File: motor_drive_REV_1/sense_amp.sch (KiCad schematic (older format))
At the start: 4 parts

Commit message: work on component libraries and schematic
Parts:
- removed C?: C, symbol Device:C
- removed R? (x2): R, symbol Device:R
- removed U?: AD8418, symbol motor_drive:AD8418
- added C?: C, symbol Device:C
- added U?: AD8418ABRMZ-RL, RM_8, symbol motor_drive:AD8418ABRMZ-RL
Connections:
- net labels added: 5.0V, OUT
- net labels removed: VCC, out
- wire segments 12 -> 10
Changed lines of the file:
@@
 $Descr A4 11693 8268
 encoding utf-8
-Sheet 9 14
+Sheet 13 14
 Title ""
 Date ""
@@
 Comment4 ""
 $EndDescr
+Text HLabel 6500 3500 2    50   Input ~ 0
+IN+
+Text HLabel 4500 3500 0    50   Input ~ 0
+IN-
 $Comp
-L Device:R R?
-U 1 1 5E23D4AE
-P 5850 1800
-AR Path="/5E1E8A88/5E23D4AE" Ref="R?"  Part="1"
-AR Path="/5E23C306/5E23D4AE" Ref="R?"  Part="1"
-AR Path="/5E285F18/5E23D4AE" Ref="R?"  Part="1"
-AR Path="/5E286BCF/5E23D4AE" Ref="R?"  Part="1"
-AR Path="/5E291A12/5E23D4AE" Ref="R?"  Part="1"
-AR Path="/5E2938C8/5E23D4AE" Ref="R?"  Part="1"
-AR Path="/5E295828/5E23D4AE" Ref="R?"  Part="1"
-AR Path="/5E2E3D6E/5E23D4AE" Ref="R?"  Part="1"
-AR Path="/5E2E5BBE/5E23D4AE" Ref="R?"  Part="1"
-AR Path="/5E2E7F62/5E23D4AE" Ref="R?"  Part="1"
-F 0 "R?" H 5920 1846 50  0000 L CNN
-F 1 "R" H 5920 1755 50  0000 L CNN
-F 2 "" V 5780 1800 50  0001 C CNN
-F 3 "~" H 5850 1800 50  0001 C CNN
-	1    5850 1800
-	1    0    0    -1
-$EndComp
-$Comp
-L Device:R R?
-U 1 1 5E23D4B4
-P 6350 1800
-AR Path="/5E1E8A88/5E23D4B4" Ref="R?"  Part="1"
-AR Path="/5E23C306/5E23D4B4" Ref="R?"  Part="1"
-AR Path="/5E285F18/5E23D4B4" Ref="R?"  Part="1"
-AR Path="/5E286BCF/5E23D4B4" Ref="R?"  Part="1"
-AR Path="/5E291A12/5E23D4B4" Ref="R?"  Part="1"
-AR Path="/5E2938C8/5E23D4B4" Ref="R?"  Part="1"
-AR Path="/5E295828/5E23D4B4" Ref="R?"  Part="1"
-AR Path="/5E2E3D6E/5E23D4B4" Ref="R?"  Part="1"
-AR Path="/5E2E5BBE/5E23D4B4" Ref="R?"  Part="1"
-AR Path="/5E2E7F62/5E23D4B4" Ref="R?"  Part="1"
-F 0 "R?" H 6420 1846 50  0000 L CNN
-F 1 "R" H 6420 1755 50  0000 L CNN
-F 2 "" V 6280 1800 50  0001 C CNN
-F 3 "~" H 6350 1800 50  0001 C CNN
-	1    6350 1800
-	1    0    0    -1
-$EndComp
-$Comp
-L Device:C C?
-U 1 1 5E23D4BA
-P 5100 4600
-AR Path="/5E1E8A88/5E23D4BA" Ref="C?"  Part="1"
-AR Path="/5E23C306/5E23D4BA" Ref="C?"  Part="1"
-AR Path="/5E285F18/5E23D4BA" Ref="C?"  Part="1"
-AR Path="/5E286BCF/5E23D4BA" Ref="C?"  Part="1"
-AR Path="/5E291A12/5E23D4BA" Ref="C?"  Part="1"
-AR Path="/5E2938C8/5E23D4BA" Ref="C?"  Part="1"
-AR Path="/5E295828/5E23D4BA" Ref="C?"  Part="1"
-AR Path="/5E2E3D6E/5E23D4BA" Ref="C?"  Part="1"
-AR Path="/5E2E5BBE/5E23D4BA" Ref="C?"  Part="1"
-AR Path="/5E2E7F62/5E23D4BA" Ref="C?"  Part="1"
-F 0 "C?" H 5215 4646 50  0000 L CNN
-F 1 "C" H 5215 4555 50  0000 L CNN
-F 2 "" H 5138 4450 50  0001 C CNN
-F 3 "~" H 5100 4600 50  0001 C CNN
-	1    5100 4600
-	0    -1   -1   0
-$EndComp
-$Comp
-L power:GND #PWR?
-U 1 1 5E23E102
-P 5850 4750
-AR Path="/5E23C306/5E23E102" Ref="#PWR?"  Part="1"
-AR Path="/5E285F18/5E23E102" Ref="#PWR?"  Part="1"
-AR Path="/5E286BCF/5E23E102" Ref="#PWR?"  Part="1"
-AR Path="/5E291A12/5E23E102" Ref="#PWR?"  Part="1"
-AR Path="/5E2938C8/5E23E102" Ref="#PWR?"  Part="1"
-AR Path="/5E295828/5E23E102" Ref="#PWR?"  Part="1"
-AR Path="/5E2E3D6E/5E23E102" Ref="#PWR?"  Part="1"
-AR Path="/5E2E5BBE/5E23E102" Ref="#PWR?"  Part="1"
-AR Path="/5E2E7F62/5E23E102" Ref="#PWR?"  Part="1"
-F 0 "#PWR?" H 5850 4500 50  0001 C CNN
-F 1 "GND" H 5855 4577 50  0000 C CNN
-F 2 "" H 5850 4750 50  0001 C CNN
-F 3 "" H 5850 4750 50  0001 C CNN
-	1    5850 4750
-	1    0    0    -1
-$EndComp
-Text HLabel 5750 3700 2    50   Input ~ 0
-out
-Wire Wire Line
-	5750 3800 5850 3800
-Wire Wire Line
-	5350 4100 5350 4600
-Wire Wire Line
-	5350 4600 5250 4600
-Wire Wire Line
-	5350 4600 5850 4600
-Connection ~ 5350 4600
-Connection ~ 5850 4600
-Wire Wire Line
-	5850 4600 5850 4750
-Wire Wire Line
-	5850 3800 5850 4600
-Wire Wire Line
-	4950 3800 4750 3800
-Wire Wire Line
-	4750 3800 4750 3900
-Wire Wire Line
-	4750 4600 4950 4600
-Wire Wire Line
-	4950 3900 4750 3900
-Connection ~ 4750 3900
-Wire Wire Line
-	4750 3900 4750 4600
-$Comp
-L power:VCC #PWR?
-U 1 1 5E2423AC
-P 4750 3600
-AR Path="/5E23C306/5E2423AC" Ref="#PWR?"  Part="1"
-AR Path="/5E285F18/5E2423AC" Ref="#PWR?"  Part="1"
-AR Path="/5E286BCF/5E2423AC" Ref="#PWR?"  Part="1"
-AR Path="/5E291A12/5E2423AC" Ref="#PWR?"  Part="1"
-AR Path="/5E2938C8/5E2423AC" Ref="#PWR?"  Part="1"
-AR Path="/5E295828/5E2423AC" Ref="#PWR?"  Part="1"
-AR Path="/5E2E3D6E/5E2423AC" Ref="#PWR?"  Part="1"
-AR Path="/5E2E5BBE/5E2423AC" Ref="#PWR?"  Part="1"
-AR Path="/5E2E7F62/5E2423AC" Ref="#PWR?"  Part="1"
-F 0 "#PWR?" H 4750 3450 50  0001 C CNN
-F 1 "VCC" H 4767 3773 50  0000 C CNN
-F 2 "" H 4750 3600 50  0001 C CNN
-F 3 "" H 4750 3600 50  0001 C CNN
-	1    4750 3600
+L motor_drive:AD8418ABRMZ-RL U?
+U 1 1 5E259F13
+P 4500 3500
+AR Path="/5E291A12/5E259F13" Ref="U?"  Part="1"
+AR Path="/5E2938C8/5E259F13" Ref="U?"  Part="1"
+AR Path="/5E295828/5E259F13" Ref="U?"  Part="1"
+AR Path="/5E2E3D6E/5E259F13" Ref="U?"  Part="1"
+AR Path="/5E2E5BBE/5E259F13" Ref="U?"  Part="1"
+AR Path="/5E2E7F62/5E259F13" Ref="U?"  Part="1"
+AR Path="/5E336639/5E259F13" Ref="U?"  Part="1"
+AR Path="/5E33A08D/5E259F13" Ref="U?"  Part="1"
+AR Path="/5E33E36D/5E259F13" Ref="U?"  Part="1"
+F 0 "U?" H 5500 3887 60  0000 C CNN
+F 1 "AD8418ABRMZ-RL" H 5500 3781 60  0000 C CNN
+F 2 "RM_8" H 5500 3740 60  0001 C CNN
+F 3 "" H 4500 3500 60  0000 C CNN
+	1    4500 3500
 	1    0    0    -1
 $EndComp
 Wire Wire Line
-	4750 3600 4750 3800
-Connection ~ 4750 3800
-Text HLabel 5150 3300 1    50   Input ~ 0
-IN+
-Text HLabel 5550 3300 1    50   Input ~ 0
-IN-
-Text HLabel 5850 4600 2    50   Input ~ 0
+	4500 3600 4100 3600
+Wire Wire Line
+	4500 3700 4100 3700
+Wire Wire Line
+	4100 3600 4100 3700
+Wire Wire Line
+	7150 3600 6500 3600
+Wire Wire Line
+	6500 3700 7150 3700
+Wire Wire Line
+	7150 3700 7150 3600
+$Comp
+L Device:C C?
+U 1 1 5E25CC80
+P 5500 4250
+AR Path="/5E1E8A88/5E25CC80" Ref="C?"  Part="1"
+AR Path="/5E23C306/5E25CC80" Ref="C?"  Part="1"
+AR Path="/5E285F18/5E25CC80" Ref="C?"  Part="1"
+AR Path="/5E286BCF/5E25CC80" Ref="C?"  Part="1"
+AR Path="/5E291A12/5E25CC80" Ref="C?"  Part="1"
+AR Path="/5E2938C8/5E25CC80" Ref="C?"  Part="1"
+AR Path="/5E295828/5E25CC80" Ref="C?"  Part="1"
+AR Path="/5E2E3D6E/5E25CC80" Ref="C?"  Part="1"
+AR Path="/5E2E5BBE/5E25CC80" Ref="C?"  Part="1"
+AR Path="/5E2E7F62/5E25CC80" Ref="C?"  Part="1"
+AR Path="/5E336639/5E25CC80" Ref="C?"  Part="1"
+AR Path="/5E33A08D/5E25CC80" Ref="C?"  Part="1"
+AR Path="/5E33E36D/5E25CC80" Ref="C?"  Part="1"
+F 0 "C?" H 5615 4296 50  0000 L CNN
+F 1 "C" H 5615 4205 50  0000 L CNN
+F 2 "" H 5538 4100 50  0001 C CNN
+F 3 "~" H 5500 4250 50  0001 C CNN
+	1    5500 4250
+	0    -1   -1   0
+$EndComp
+Wire Wire Line
+	4100 3700 4100 4250
+Connection ~ 4100 3700
+Wire Wire Line
+	5350 4250 4100 4250
+Wire Wire Line
+	5650 4250 7150 4250
+Wire Wire Line
+	7150 4250 7150 3700
+Connection ~ 7150 3700
+Text HLabel 6500 3800 2    50   Input ~ 0
+OUT
+Text HLabel 7150 3600 2    50   Input ~ 0
+5.0V
+Text HLabel 4100 4250 0    50   Input ~ 0
 GND
-Text HLabel 4750 3800 0    50   Input ~ 0
-VCC
-$Comp
-L motor_drive:AD8418 U?
-U 1 1 5E24089B
-P 5350 3700
-F 0 "U?" H 5350 3211 50  0000 C CNN
-F 1 "AD8418" H 5350 3120 50  0000 C CNN
-F 2 "" H 5400 3350 50  0001 C CNN
-F 3 "https://www.analog.com/media/en/technical-documentation/data-sheets/AD8418.pdf" H 6000 3000 50  0001 C CNN
-	1    5350 3700
-	1    0    0    -1
-$EndComp
 $EndSCHEMATC

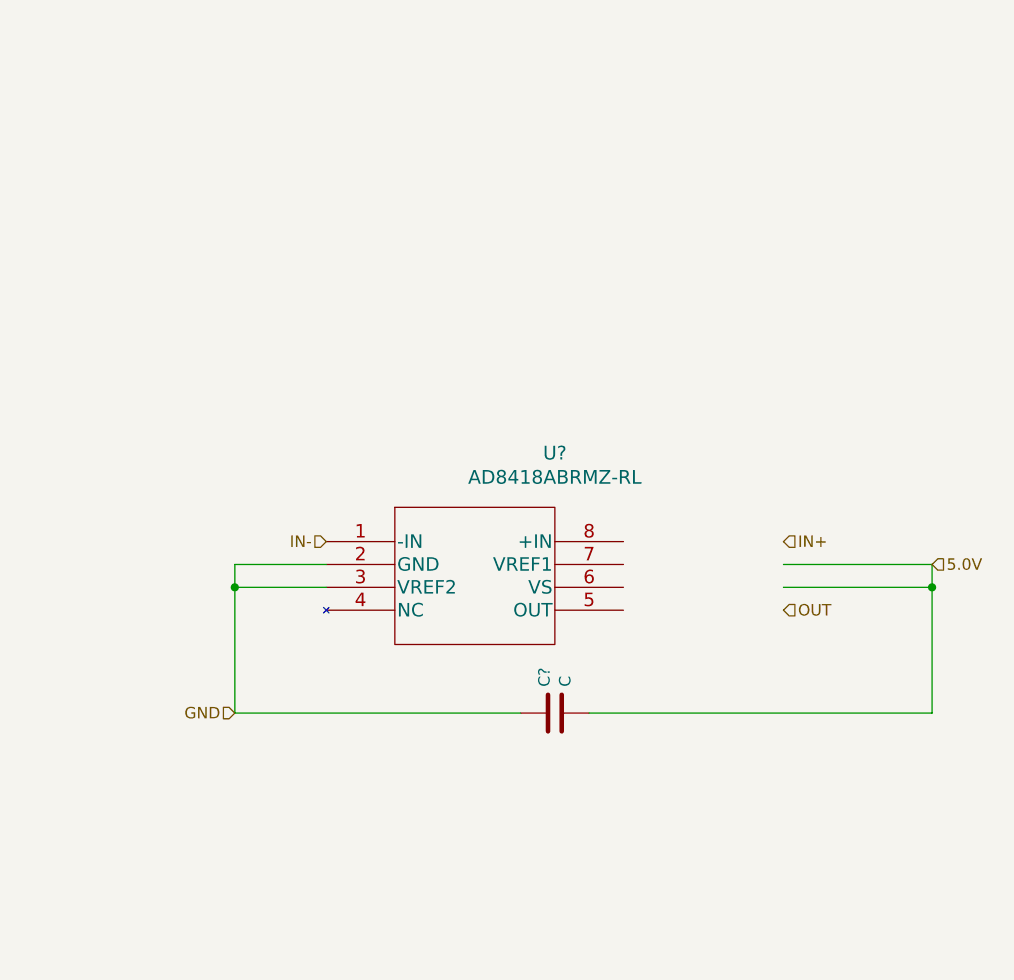
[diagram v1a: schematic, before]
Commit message: organizing pinout and BOM
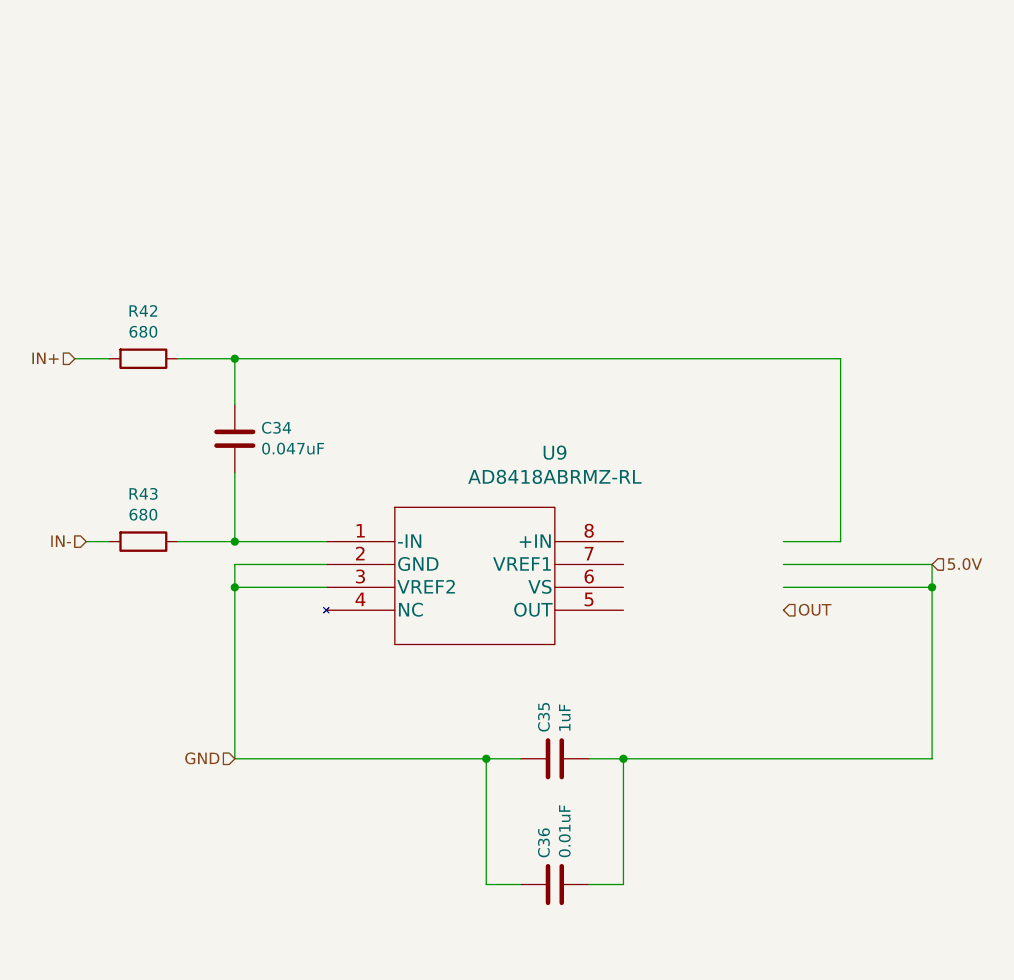
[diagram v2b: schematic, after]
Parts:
- added C1: 0.047uF, motor_drive_footprints:C_0603_1608Metric, symbol motor_drive:C
- added C36: 0.01uF, motor_drive_footprints:C_0603_1608Metric, symbol Device:C
- added R10, R11: 680, motor_drive_footprints:C_0603_1608Metric, symbol motor_drive:R
- C35: renamed from C?; value C -> 1uF; footprint (none) -> motor_drive_footprints:C_0603_1608Metric
- U9: renamed from U?; footprint RM_8 -> motor_drive_footprints:AD8418ABRMZ-RL
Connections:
- wire segments 10 -> 26
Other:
- moved on the sheet: C35
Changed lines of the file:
@@
 $Descr A4 11693 8268
 encoding utf-8
-Sheet 13 14
+Sheet 14 14
 Title ""
 Date ""
@@
 Comment4 ""
 $EndDescr
-Text HLabel 6500 3500 2    50   Input ~ 0
+Text HLabel 3400 2700 0    50   Input ~ 0
 IN+
-Text HLabel 4500 3500 0    50   Input ~ 0
-IN-
-$Comp
-L motor_drive:AD8418ABRMZ-RL U?
+$Comp
+L motor_drive:AD8418ABRMZ-RL U9
 U 1 1 5E259F13
 P 4500 3500
-AR Path="/5E291A12/5E259F13" Ref="U?"  Part="1"
-AR Path="/5E2938C8/5E259F13" Ref="U?"  Part="1"
-AR Path="/5E295828/5E259F13" Ref="U?"  Part="1"
+AR Path="/5E291A12/5E259F13" Ref="U9"  Part="1"
+AR Path="/5E2938C8/5E259F13" Ref="U1"  Part="1"
+AR Path="/5E295828/5E259F13" Ref="U2"  Part="1"
 AR Path="/5E2E3D6E/5E259F13" Ref="U?"  Part="1"
 AR Path="/5E2E5BBE/5E259F13" Ref="U?"  Part="1"
 AR Path="/5E2E7F62/5E259F13" Ref="U?"  Part="1"
-AR Path="/5E336639/5E259F13" Ref="U?"  Part="1"
-AR Path="/5E33A08D/5E259F13" Ref="U?"  Part="1"
+AR Path="/5E336639/5E259F13" Ref="U3"  Part="1"
+AR Path="/5E33A08D/5E259F13" Ref="U4"  Part="1"
 AR Path="/5E33E36D/5E259F13" Ref="U?"  Part="1"
-F 0 "U?" H 5500 3887 60  0000 C CNN
+F 0 "U9" H 5500 3887 60  0000 C CNN
 F 1 "AD8418ABRMZ-RL" H 5500 3781 60  0000 C CNN
-F 2 "RM_8" H 5500 3740 60  0001 C CNN
+F 2 "motor_drive_footprints:AD8418ABRMZ-RL" H 5500 3740 60  0001 C CNN
 F 3 "" H 4500 3500 60  0000 C CNN
 	1    4500 3500
@@
 L Device:C C?
 U 1 1 5E25CC80
-P 5500 4250
+P 5500 4450
 AR Path="/5E1E8A88/5E25CC80" Ref="C?"  Part="1"
 AR Path="/5E23C306/5E25CC80" Ref="C?"  Part="1"
 AR Path="/5E285F18/5E25CC80" Ref="C?"  Part="1"
 AR Path="/5E286BCF/5E25CC80" Ref="C?"  Part="1"
-AR Path="/5E291A12/5E25CC80" Ref="C?"  Part="1"
-AR Path="/5E2938C8/5E25CC80" Ref="C?"  Part="1"
-AR Path="/5E295828/5E25CC80" Ref="C?"  Part="1"
+AR Path="/5E291A12/5E25CC80" Ref="C35"  Part="1"
+AR Path="/5E2938C8/5E25CC80" Ref="C2"  Part="1"
+AR Path="/5E295828/5E25CC80" Ref="C5"  Part="1"
 AR Path="/5E2E3D6E/5E25CC80" Ref="C?"  Part="1"
 AR Path="/5E2E5BBE/5E25CC80" Ref="C?"  Part="1"
 AR Path="/5E2E7F62/5E25CC80" Ref="C?"  Part="1"
-AR Path="/5E336639/5E25CC80" Ref="C?"  Part="1"
-AR Path="/5E33A08D/5E25CC80" Ref="C?"  Part="1"
+AR Path="/5E336639/5E25CC80" Ref="C8"  Part="1"
+AR Path="/5E33A08D/5E25CC80" Ref="C11"  Part="1"
 AR Path="/5E33E36D/5E25CC80" Ref="C?"  Part="1"
-F 0 "C?" H 5615 4296 50  0000 L CNN
-F 1 "C" H 5615 4205 50  0000 L CNN
-F 2 "" H 5538 4100 50  0001 C CNN
-F 3 "~" H 5500 4250 50  0001 C CNN
-	1    5500 4250
+F 0 "C35" H 5615 4496 50  0000 L CNN
+F 1 "1uF" H 5615 4405 50  0000 L CNN
+F 2 "motor_drive_footprints:C_0603_1608Metric" H 5538 4300 50  0001 C CNN
+F 3 "~" H 5500 4450 50  0001 C CNN
+	1    5500 4450
 	0    -1   -1   0
 $EndComp
-Wire Wire Line
-	4100 3700 4100 4250
-Connection ~ 4100 3700
-Wire Wire Line
-	5350 4250 4100 4250
-Wire Wire Line
-	5650 4250 7150 4250
-Wire Wire Line
-	7150 4250 7150 3700
-Connection ~ 7150 3700
 Text HLabel 6500 3800 2    50   Input ~ 0
 OUT
 Text HLabel 7150 3600 2    50   Input ~ 0
 5.0V
-Text HLabel 4100 4250 0    50   Input ~ 0
+Text HLabel 4100 4450 0    50   Input ~ 0
 GND
+Wire Wire Line
+	6500 3500 6750 3500
+Wire Wire Line
+	7150 3700 7150 4450
+Connection ~ 7150 3700
+Wire Wire Line
+	4100 3700 4100 4450
+Connection ~ 4100 3700
+$Comp
+L Device:C C?
+U 1 1 5E3A2D2D
+P 5500 5000
+AR Path="/5E1E8A88/5E3A2D2D" Ref="C?"  Part="1"
+AR Path="/5E23C306/5E3A2D2D" Ref="C?"  Part="1"
+AR Path="/5E285F18/5E3A2D2D" Ref="C?"  Part="1"
+AR Path="/5E286BCF/5E3A2D2D" Ref="C?"  Part="1"
+AR Path="/5E291A12/5E3A2D2D" Ref="C36"  Part="1"
+AR Path="/5E2938C8/5E3A2D2D" Ref="C3"  Part="1"
+AR Path="/5E295828/5E3A2D2D" Ref="C6"  Part="1"
+AR Path="/5E2E3D6E/5E3A2D2D" Ref="C?"  Part="1"
+AR Path="/5E2E5BBE/5E3A2D2D" Ref="C?"  Part="1"
+AR Path="/5E2E7F62/5E3A2D2D" Ref="C?"  Part="1"
+AR Path="/5E336639/5E3A2D2D" Ref="C9"  Part="1"
+AR Path="/5E33A08D/5E3A2D2D" Ref="C12"  Part="1"
+AR Path="/5E33E36D/5E3A2D2D" Ref="C?"  Part="1"
+F 0 "C36" H 5615 5046 50  0000 L CNN
+F 1 "0.01uF" H 5615 4955 50  0000 L CNN
+F 2 "motor_drive_footprints:C_0603_1608Metric" H 5538 4850 50  0001 C CNN
+F 3 "~" H 5500 5000 50  0001 C CNN
+	1    5500 5000
+	0    -1   -1   0
+$EndComp
+Wire Wire Line
+	5650 5000 5800 5000
+Wire Wire Line
+	5350 5000 5200 5000
+Wire Wire Line
+	4100 4450 5200 4450
+Wire Wire Line
+	5650 4450 5800 4450
+Wire Wire Line
+	5800 4450 5800 5000
+Connection ~ 5800 4450
+Wire Wire Line
+	5800 4450 7150 4450
+Wire Wire Line
+	5200 4450 5200 5000
+Connection ~ 5200 4450
+Wire Wire Line
+	5200 4450 5350 4450
+Text HLabel 3450 3500 0    50   Input ~ 0
+IN-
+$Comp
+L motor_drive:R R?
+U 1 1 5E3B6CAC
+P 3700 2700
+AR Path="/5E26944C/5E3B6CAC" Ref="R?"  Part="1"
+AR Path="/5E3B6CAC" Ref="R?"  Part="1"
+AR Path="/5E334D58/5E3B6CAC" Ref="R?"  Part="1"
+AR Path="/5E2938C8/5E3B6CAC" Ref="R10"  Part="1"
+AR Path="/5E295828/5E3B6CAC" Ref="R12"  Part="1"
+AR Path="/5E336639/5E3B6CAC" Ref="R14"  Part="1"
+AR Path="/5E33A08D/5E3B6CAC" Ref="R16"  Part="1"
+AR Path="/5E291A12/5E3B6CAC" Ref="R42"  Part="1"
+F 0 "R42" V 3493 2700 50  0000 C CNN
+F 1 "680" V 3584 2700 50  0000 C CNN
+F 2 "motor_drive_footprints:C_0603_1608Metric" V 3630 2700 50  0001 C CNN
+F 3 "~" H 3700 2700 50  0001 C CNN
+	1    3700 2700
+	0    1    1    0
+$EndComp
+$Comp
+L motor_drive:C C?
+U 1 1 5E3B79F8
+P 4100 3050
+AR Path="/5E38D632/5E3B79F8" Ref="C?"  Part="1"
+AR Path="/5E334D58/5E3B79F8" Ref="C?"  Part="1"
+AR Path="/5E2938C8/5E3B79F8" Ref="C1"  Part="1"
+AR Path="/5E295828/5E3B79F8" Ref="C4"  Part="1"
+AR Path="/5E336639/5E3B79F8" Ref="C7"  Part="1"
+AR Path="/5E33A08D/5E3B79F8" Ref="C10"  Part="1"
+AR Path="/5E291A12/5E3B79F8" Ref="C34"  Part="1"
+F 0 "C34" H 4215 3096 50  0000 L CNN
+F 1 "0.047uF" H 4215 3005 50  0000 L CNN
+F 2 "motor_drive_footprints:C_0603_1608Metric" H 4138 2900 50  0001 C CNN
+F 3 "~" H 4100 3050 50  0001 C CNN
+	1    4100 3050
+	1    0    0    -1
+$EndComp
+Wire Wire Line
+	3400 2700 3550 2700
+Wire Wire Line
+	3850 2700 4100 2700
+Wire Wire Line
+	4100 2700 6750 2700
+Wire Wire Line
+	6750 2700 6750 3500
+Connection ~ 4100 2700
+Wire Wire Line
+	4100 2700 4100 2900
+Wire Wire Line
+	4100 3200 4100 3500
+Wire Wire Line
+	4100 3500 4500 3500
+$Comp
+L motor_drive:R R?
+U 1 1 5E394586
+P 3700 3500
+AR Path="/5E26944C/5E394586" Ref="R?"  Part="1"
+AR Path="/5E394586" Ref="R?"  Part="1"
+AR Path="/5E334D58/5E394586" Ref="R?"  Part="1"
+AR Path="/5E2938C8/5E394586" Ref="R11"  Part="1"
+AR Path="/5E295828/5E394586" Ref="R13"  Part="1"
+AR Path="/5E336639/5E394586" Ref="R15"  Part="1"
+AR Path="/5E33A08D/5E394586" Ref="R17"  Part="1"
+AR Path="/5E291A12/5E394586" Ref="R43"  Part="1"
+F 0 "R43" V 3493 3500 50  0000 C CNN
+F 1 "680" V 3584 3500 50  0000 C CNN
+F 2 "motor_drive_footprints:C_0603_1608Metric" V 3630 3500 50  0001 C CNN
+F 3 "~" H 3700 3500 50  0001 C CNN
+	1    3700 3500
+	0    1    1    0
+$EndComp
+Wire Wire Line
+	3850 3500 4100 3500
+Connection ~ 4100 3500
+Wire Wire Line
+	3550 3500 3450 3500
 $EndSCHEMATC
